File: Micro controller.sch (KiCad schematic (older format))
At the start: 31 parts, among them J1 USB_B, U1 BAT54C, U14 ferrite, U20 TPD3S014, U21 MKL02Z32VFG4, U22 LP38691, U23 MK66FX1M0, U3 ferrite, U5 ferrite, U6 BAT54C, Y1 Crystal_16MHz, Y2 32.768MHz

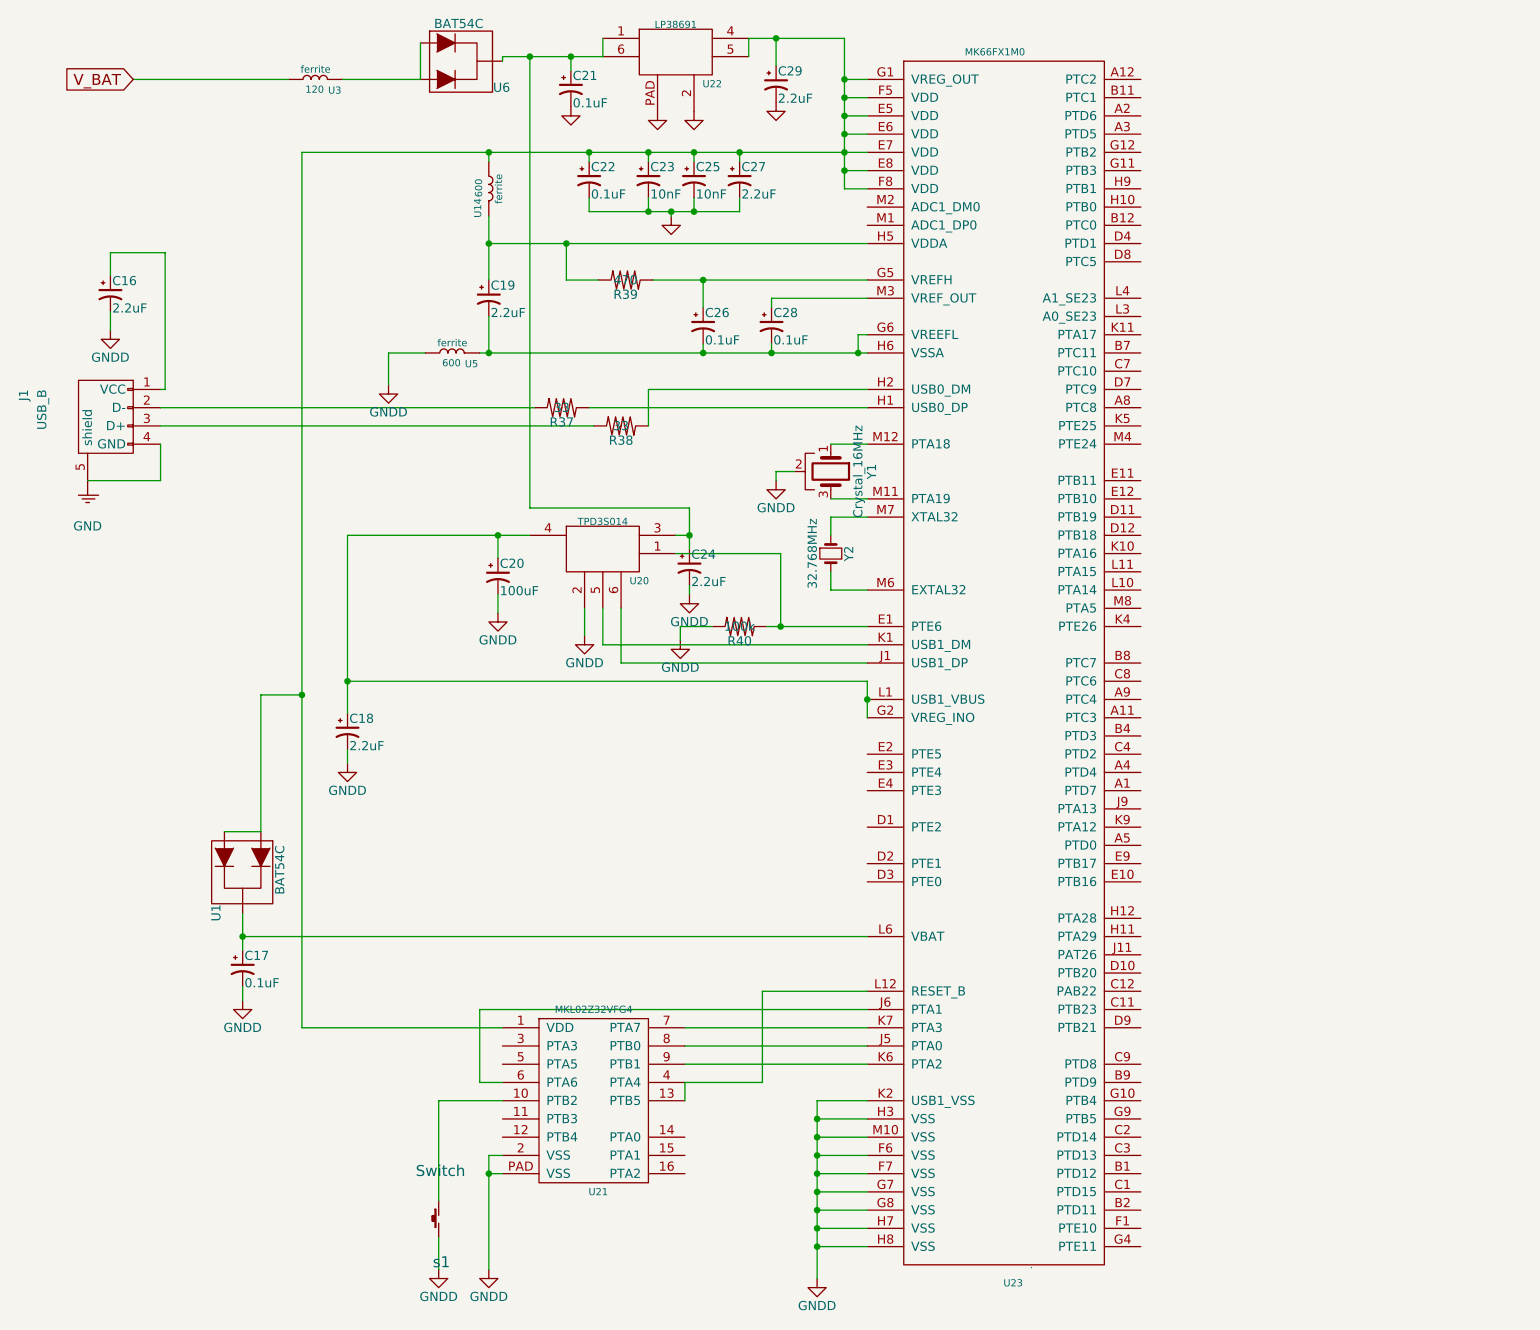
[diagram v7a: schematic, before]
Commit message: wired up the MCU
-wired up the mcu to the gyro, motor controller.
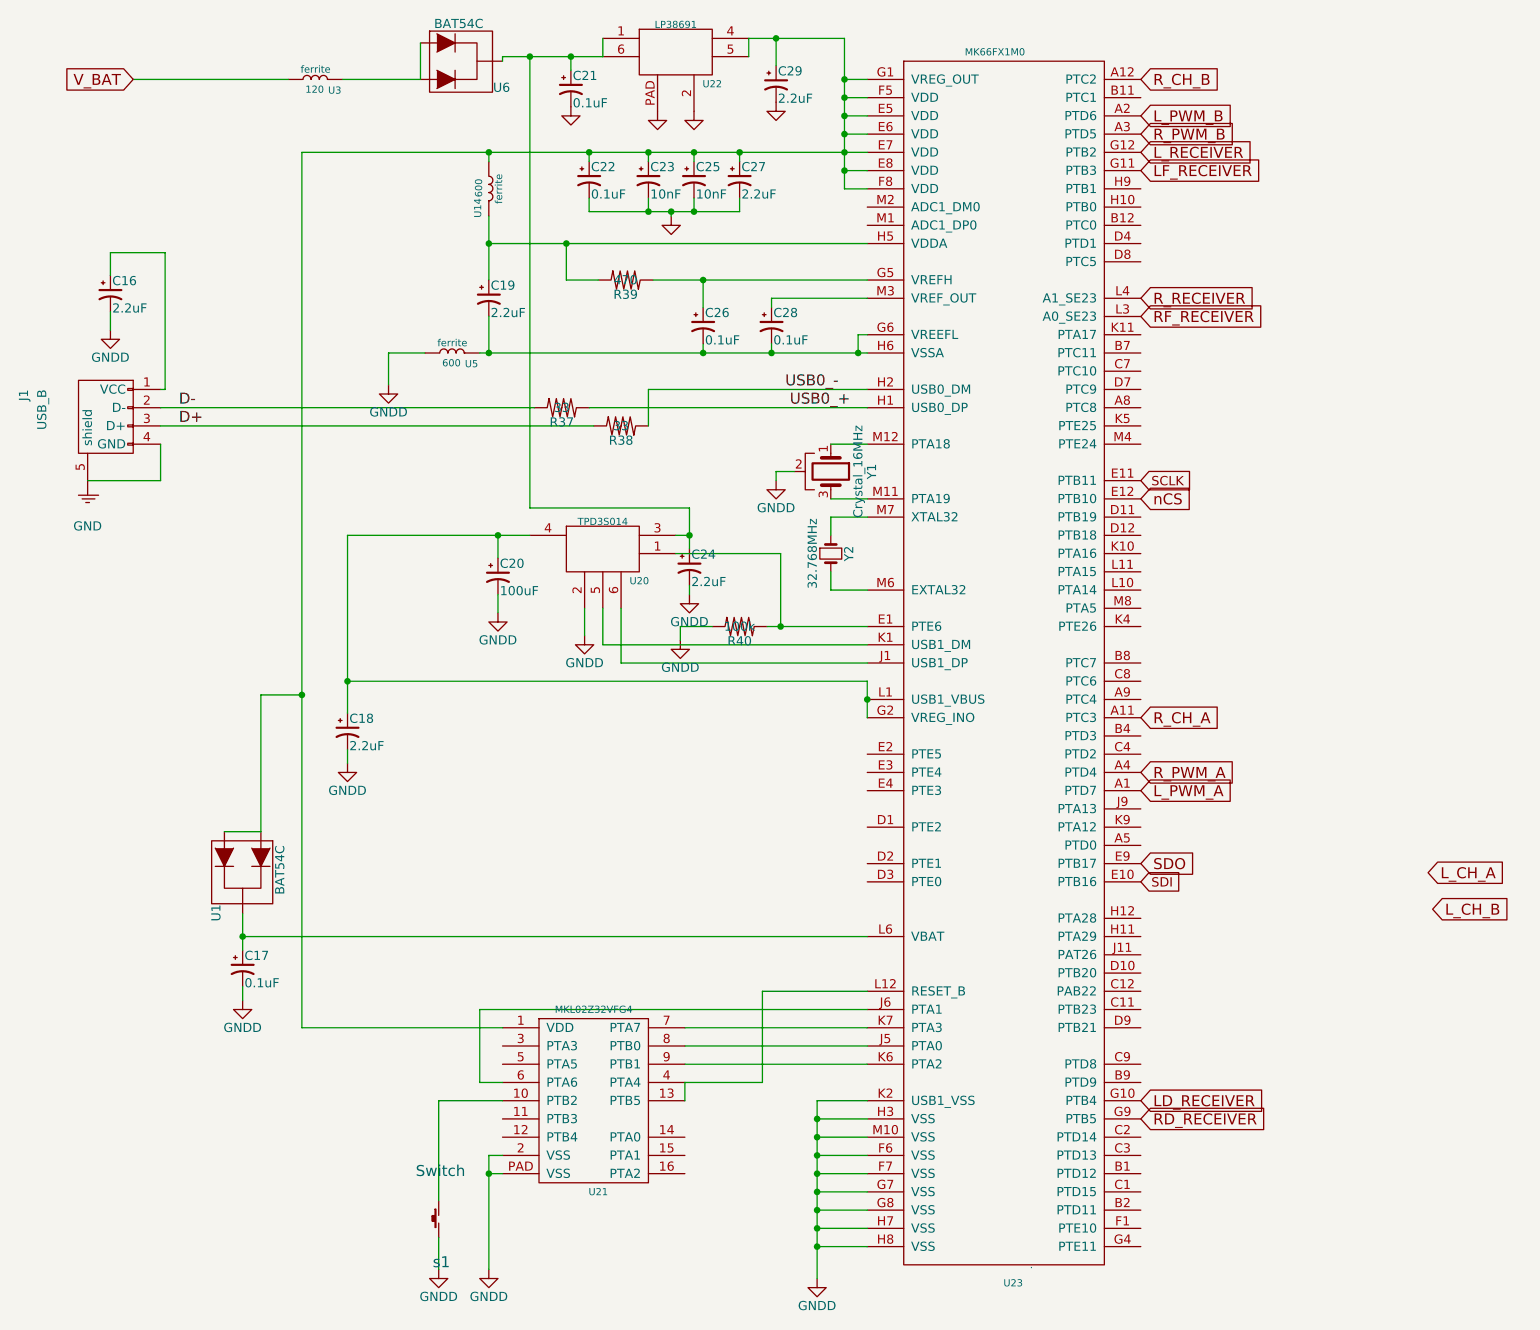
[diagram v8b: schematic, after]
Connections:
- net L_PWM_A: now reaches U23.A1 (PTD7)
- net R_CH_A: now reaches U23.A11 (PTC3)
- net R_CH_B: now reaches U23.A12 (PTC2)
- net L_PWM_B: now reaches U23.A2 (PTD6)
- net R_PWM_B: now reaches U23.A3 (PTD5)
- net R_PWM_A: now reaches U23.A4 (PTD4)
- net SDI: now reaches U23.E10 (PTB16)
- net SCLK: now reaches U23.E11 (PTB11)
- net nCS: now reaches U23.E12 (PTB10)
- net SDO: now reaches U23.E9 (PTB17)
- net LD_RECEIVER: now reaches U23.G10 (PTB4)
- net LF_RECEIVER: now reaches U23.G11 (PTB3)
- net L_RECEIVER: now reaches U23.G12 (PTB2)
- net RD_RECEIVER: now reaches U23.G9 (PTB5)
- net USB0_+: now reaches R37.1, U23.H1 (USB0_DP)
- net USB0_-: now reaches R38.1, U23.H2 (USB0_DM)
- net RF_RECEIVER: now reaches U23.L3 (A0_SE23)
- net R_RECEIVER: now reaches U23.L4 (A1_SE23)
- net D-: now reaches J1.2 (D-), R37.2
- net D+: now reaches J1.3 (D+), R38.2
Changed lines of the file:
@@
-$EndComp
-$Comp
-L BAT54C U6
-U 1 1 59498B94
-P 2875 625
-F 0 "U6" H 3170 380 50  0000 C CNN
-F 1 "BAT54C" H 2935 730 50  0000 C CNN
-F 2 "micromouse:PMEG4010_DIODE" H 2955 175 50  0001 C CNN
-F 3 "" H 2875 725 50  0000 C CNN
-F 4 "BAT54C" H 2945 285 60  0001 C CNN "manf#"
-	1    2875 625
-	1    0    0    -1
 $EndComp
 $Comp
@@
 $EndComp
 $Comp
-L GNDD #PWR32
+L GNDD #PWR030
 U 1 1 594A0F24
 P 1025 2200
-F 0 "#PWR32" H 1025 1950 50  0001 C CNN
+F 0 "#PWR030" H 1025 1950 50  0001 C CNN
 F 1 "GNDD" H 1025 2050 50  0000 C CNN
 F 2 "" H 1025 2200 50  0001 C CNN
@@
 $EndComp
 $Comp
-L GNDD #PWR48
+L GNDD #PWR031
 U 1 1 594A2D63
 P 4900 7400
-F 0 "#PWR48" H 4900 7150 50  0001 C CNN
+F 0 "#PWR031" H 4900 7150 50  0001 C CNN
 F 1 "GNDD" H 4900 7250 50  0000 C CNN
 F 2 "" H 4900 7400 50  0001 C CNN
@@
 	1    4900 7400
 	1    0    0    -1
-$EndComp
-$Comp
-L BAT54C U1
-U 1 1 594A3A49
-P 1850 5100
-F 0 "U1" H 2145 4855 50  0000 C CNN
-F 1 "BAT54C" H 1910 5205 50  0000 C CNN
-F 2 "micromouse:PMEG4010_DIODE" H 1930 4650 50  0001 C CNN
-F 3 "" H 1850 5200 50  0000 C CNN
-F 4 "BAT54C" H 1920 4760 60  0001 C CNN "manf#"
-	1    1850 5100
-	0    1    1    0
 $EndComp
 $Comp
@@
 $EndComp
 $Comp
-L GNDD #PWR33
+L GNDD #PWR032
 U 1 1 594A3CA9
 P 1750 5875
-F 0 "#PWR33" H 1750 5625 50  0001 C CNN
+F 0 "#PWR032" H 1750 5625 50  0001 C CNN
 F 1 "GNDD" H 1750 5725 50  0000 C CNN
 F 2 "" H 1750 5875 50  0001 C CNN
@@
 $EndComp
 $Comp
-L GNDD #PWR37
+L GNDD #PWR033
 U 1 1 594A4083
 P 3100 7350
-F 0 "#PWR37" H 3100 7100 50  0001 C CNN
+F 0 "#PWR033" H 3100 7100 50  0001 C CNN
 F 1 "GNDD" H 3100 7200 50  0000 C CNN
 F 2 "" H 3100 7350 50  0001 C CNN
@@
 $EndComp
 $Comp
-L GNDD #PWR36
+L GNDD #PWR034
 U 1 1 594A40CA
 P 2825 7350
-F 0 "#PWR36" H 2825 7100 50  0001 C CNN
+F 0 "#PWR034" H 2825 7100 50  0001 C CNN
 F 1 "GNDD" H 2825 7200 50  0000 C CNN
 F 2 "" H 2825 7350 50  0001 C CNN
@@
 $EndComp
 $Comp
-L GNDD #PWR35
+L GNDD #PWR035
 U 1 1 594A46C4
 P 2550 2500
-F 0 "#PWR35" H 2550 2250 50  0001 C CNN
+F 0 "#PWR035" H 2550 2250 50  0001 C CNN
 F 1 "GNDD" H 2550 2350 50  0000 C CNN
 F 2 "" H 2550 2500 50  0001 C CNN
@@
 $EndComp
 $Comp
-L GNDD #PWR43
+L GNDD #PWR036
 U 1 1 594A5B36
 P 4150 3900
-F 0 "#PWR43" H 4150 3650 50  0001 C CNN
+F 0 "#PWR036" H 4150 3650 50  0001 C CNN
 F 1 "GNDD" H 4150 3750 50  0000 C CNN
 F 2 "" H 4150 3900 50  0001 C CNN
@@
 $EndComp
 $Comp
-L GNDD #PWR38
+L GNDD #PWR037
 U 1 1 594A6698
 P 3150 3750
-F 0 "#PWR38" H 3150 3500 50  0001 C CNN
+F 0 "#PWR037" H 3150 3500 50  0001 C CNN
 F 1 "GNDD" H 3150 3600 50  0000 C CNN
 F 2 "" H 3150 3750 50  0001 C CNN
@@
 $EndComp
 $Comp
-L GNDD #PWR40
+L GNDD #PWR038
 U 1 1 594A68B7
 P 3625 3875
-F 0 "#PWR40" H 3625 3625 50  0001 C CNN
+F 0 "#PWR038" H 3625 3625 50  0001 C CNN
 F 1 "GNDD" H 3625 3725 50  0000 C CNN
 F 2 "" H 3625 3875 50  0001 C CNN
@@
 $EndComp
 $Comp
-L GNDD #PWR34
+L GNDD #PWR039
 U 1 1 594A75BB
 P 2325 4575
-F 0 "#PWR34" H 2325 4325 50  0001 C CNN
+F 0 "#PWR039" H 2325 4325 50  0001 C CNN
 F 1 "GNDD" H 2325 4425 50  0000 C CNN
 F 2 "" H 2325 4575 50  0001 C CNN
@@
 $EndComp
 $Comp
-L GNDD #PWR44
+L GNDD #PWR040
 U 1 1 594A7E36
 P 4200 3650
-F 0 "#PWR44" H 4200 3400 50  0001 C CNN
+F 0 "#PWR040" H 4200 3400 50  0001 C CNN
 F 1 "GNDD" H 4200 3500 50  0000 C CNN
 F 2 "" H 4200 3650 50  0001 C CNN
@@
 $EndComp
 $Comp
-L GNDD #PWR47
+L GNDD #PWR041
 U 1 1 598926F4
 P 4675 3025
-F 0 "#PWR47" H 4675 2775 50  0001 C CNN
+F 0 "#PWR041" H 4675 2775 50  0001 C CNN
 F 1 "GNDD" H 4675 2875 50  0000 C CNN
 F 2 "" H 4675 3025 50  0001 C CNN
@@
 $EndComp
 $Comp
-L GNDD #PWR39
+L GNDD #PWR042
 U 1 1 59B01514
 P 3550 975
-F 0 "#PWR39" H 3550 725 50  0001 C CNN
+F 0 "#PWR042" H 3550 725 50  0001 C CNN
 F 1 "GNDD" H 3550 825 50  0001 C CNN
 F 2 "" H 3550 975 50  0001 C CNN
@@
 $EndComp
 $Comp
-L GNDD #PWR46
+L GNDD #PWR043
 U 1 1 59B01D17
 P 4675 950
-F 0 "#PWR46" H 4675 700 50  0001 C CNN
+F 0 "#PWR043" H 4675 700 50  0001 C CNN
 F 1 "GNDD" H 4675 800 50  0001 C CNN
 F 2 "" H 4675 950 50  0001 C CNN
@@
 $EndComp
 $Comp
-L GNDD #PWR45
+L GNDD #PWR044
 U 1 1 59B01D7F
 P 4225 1000
-F 0 "#PWR45" H 4225 750 50  0001 C CNN
+F 0 "#PWR044" H 4225 750 50  0001 C CNN
 F 1 "GNDD" H 4225 850 50  0001 C CNN
 F 2 "" H 4225 1000 50  0001 C CNN
@@
 $EndComp
 $Comp
-L GNDD #PWR41
+L GNDD #PWR045
 U 1 1 59B01DE7
 P 4025 1000
-F 0 "#PWR41" H 4025 750 50  0001 C CNN
+F 0 "#PWR045" H 4025 750 50  0001 C CNN
 F 1 "GNDD" H 4025 850 50  0001 C CNN
 F 2 "" H 4025 1000 50  0001 C CNN
@@
 Connection ~ 5050 825
 $Comp
-L GNDD #PWR42
+L GNDD #PWR046
 U 1 1 59B0898A
 P 4100 1575
-F 0 "#PWR42" H 4100 1325 50  0001 C CNN
+F 0 "#PWR046" H 4100 1325 50  0001 C CNN
 F 1 "GNDD" H 4100 1425 50  0001 C CNN
 F 2 "" H 4100 1575 50  0001 C CNN
@@
 $EndComp
 $Comp
-L GND #PWR31
+L GND #PWR30
 U 1 1 594A1F04
 P 900 3125
-F 0 "#PWR31" H 900 2875 50  0001 C CNN
+F 0 "#PWR30" H 900 2875 50  0001 C CNN
 F 1 "GND" H 900 2975 50  0000 C CNN
 F 2 "" H 900 3125 50  0001 C CNN
@@
 Wire Wire Line
 	4600 5825 5175 5825
+$Comp
+L BAT54C U1
+U 1 1 59F0D4F4
+P 1850 5100
+F 0 "U1" H 2145 4855 50  0000 C CNN
+F 1 "BAT54C" H 1910 5205 50  0000 C CNN
+F 2 "micromouse:PMEG4010_DIODE" H 1930 4650 50  0001 C CNN
+F 3 "" H 1850 5200 50  0000 C CNN
+F 4 "BAT54C" H 1920 4760 60  0001 C CNN "manf#"
+	1    1850 5100
+	0    1    1    0
+$EndComp
+$Comp
+L BAT54C U6
+U 1 1 59F0D619
+P 2875 625
+F 0 "U6" H 3170 380 50  0000 C CNN
+F 1 "BAT54C" H 2935 730 50  0000 C CNN
+F 2 "micromouse:PMEG4010_DIODE" H 2955 175 50  0001 C CNN
+F 3 "" H 2875 725 50  0000 C CNN
+F 4 "BAT54C" H 2945 285 60  0001 C CNN "manf#"
+	1    2875 625
+	1    0    0    -1
+$EndComp
+Text GLabel 6675 5225 2    51   Input ~ 0
+SDI
+Text GLabel 6675 3025 2    51   Input ~ 0
+SCLK
+Text GLabel 6675 3125 2    60   Input ~ 0
+nCS
+Text GLabel 6675 5125 2    60   Input ~ 0
+SDO
+Text Label 4725 2525 0    60   ~ 0
+USB0_-
+Text Label 4750 2625 0    60   ~ 0
+USB0_+
+Text Label 1400 2625 0    60   ~ 0
+D-
+Text Label 1400 2725 0    60   ~ 0
+D+
+Text GLabel 6675 4625 2    60   Input ~ 0
+R_PWM_A
+Text GLabel 6675 1125 2    60   Input ~ 0
+R_PWM_B
+Text GLabel 6675 1025 2    60   Input ~ 0
+L_PWM_B
+Text GLabel 6675 4725 2    60   Input ~ 0
+L_PWM_A
+Text GLabel 6675 4325 2    60   Input ~ 0
+R_CH_A
+Text GLabel 6675 825  2    60   Input ~ 0
+R_CH_B
+Text GLabel 8250 5175 2    60   Input ~ 0
+L_CH_A
+Text GLabel 8275 5375 2    60   Input ~ 0
+L_CH_B
+Text GLabel 6675 1225 2    60   Input ~ 0
+L_RECEIVER
+Text GLabel 6675 2025 2    60   Input ~ 0
+R_RECEIVER
+Text GLabel 6675 6425 2    60   Input ~ 0
+LD_RECEIVER
+Text GLabel 6675 1325 2    60   Input ~ 0
+LF_RECEIVER
+Text GLabel 6675 6525 2    60   Input ~ 0
+RD_RECEIVER
+Text GLabel 6675 2125 2    60   Input ~ 0
+RF_RECEIVER
 $EndSCHEMATC
